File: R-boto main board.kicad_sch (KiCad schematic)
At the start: 1 part

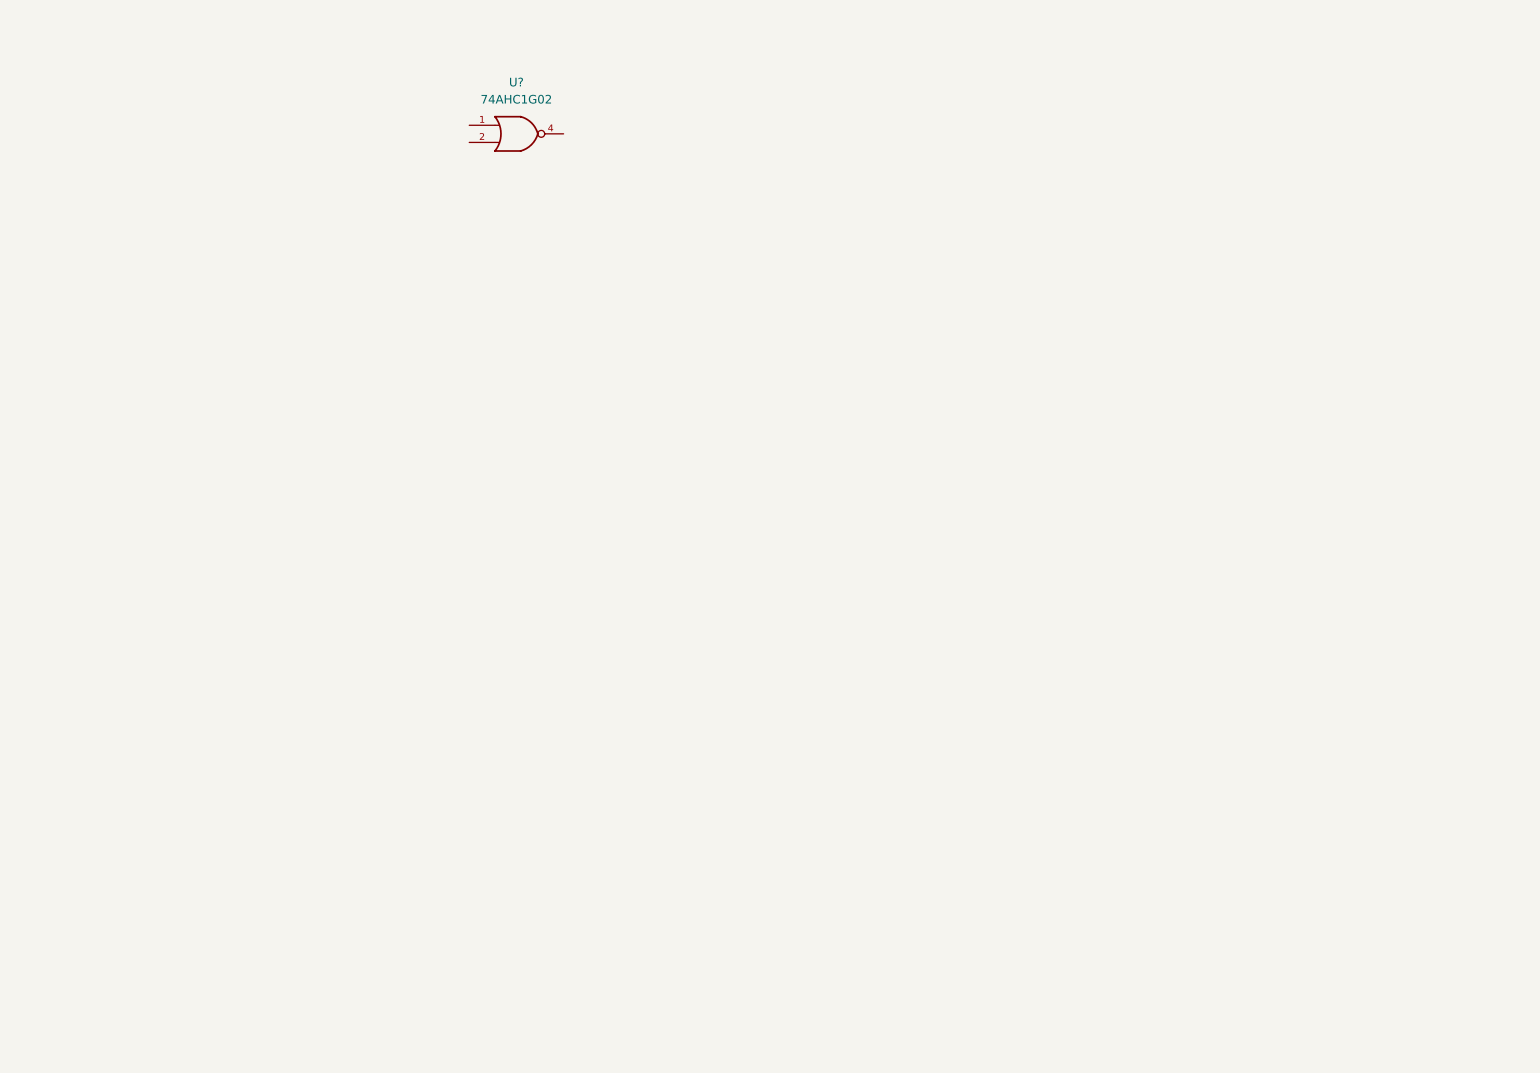
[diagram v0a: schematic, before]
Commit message: schematic connector add
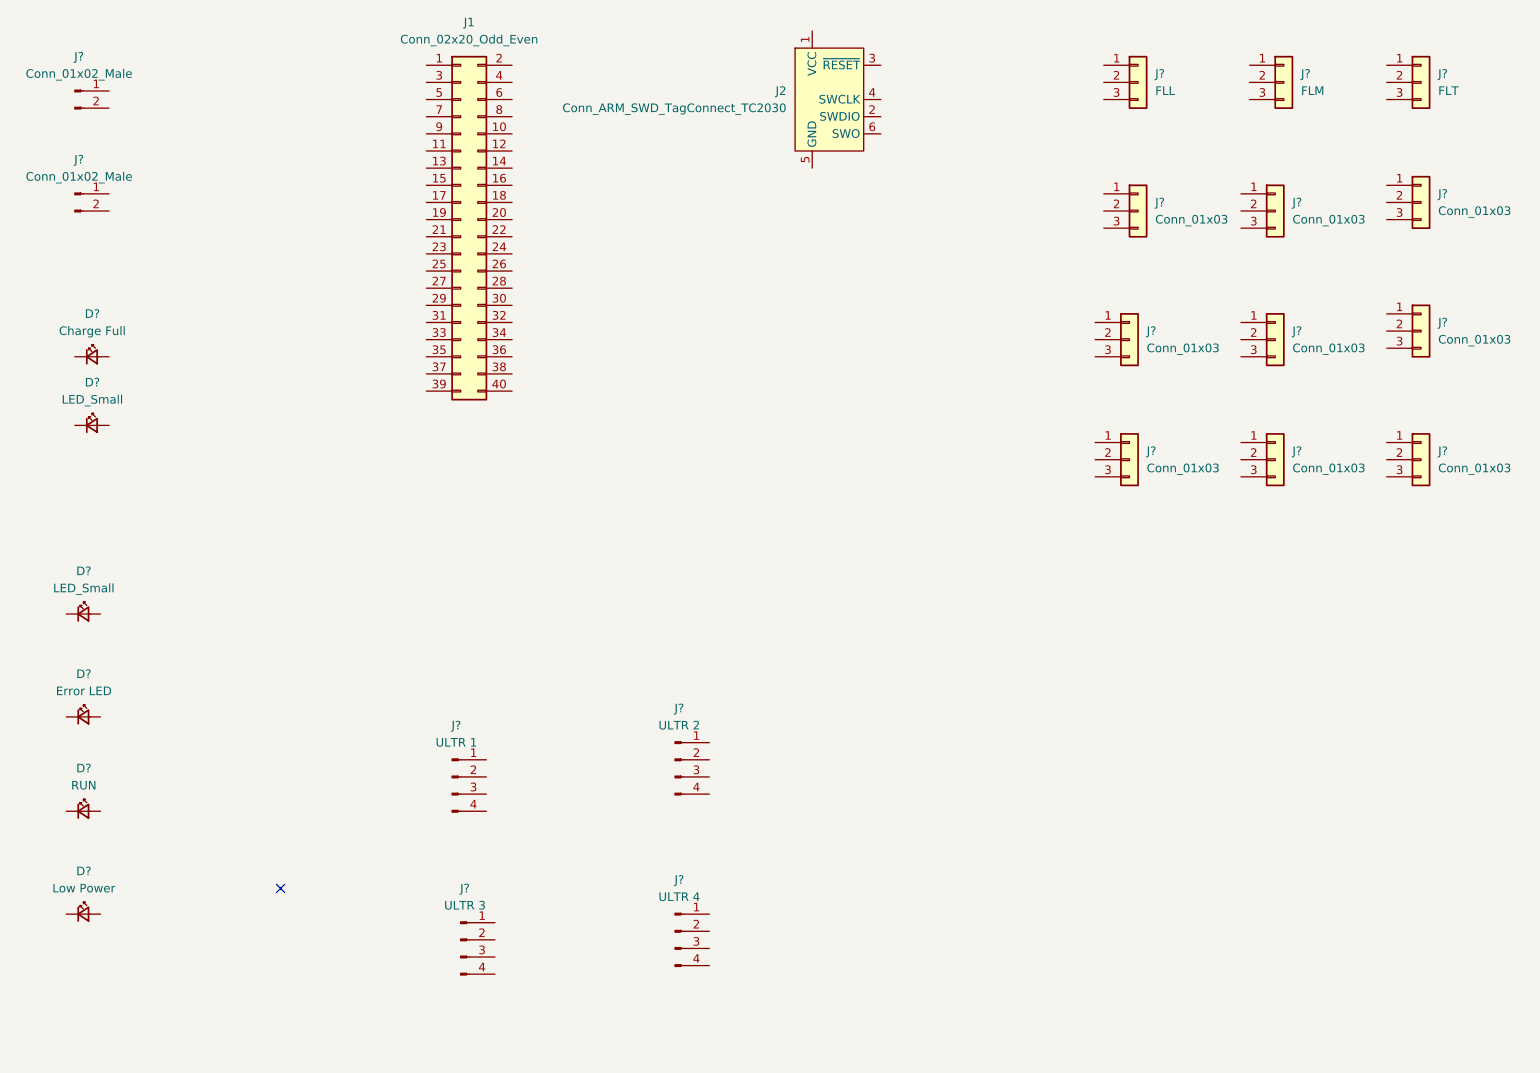
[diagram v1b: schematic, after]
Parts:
- removed U?: 74AHC1G02, symbol 74xGxx:74AHC1G02
- added D?: Charge Full, symbol Device:LED_Small
- added D? (x2): LED_Small, symbol Device:LED_Small
- added D?: Error LED, symbol Device:LED_Small
- added D?: Low Power, symbol Device:LED_Small
- added D?: RUN, symbol Device:LED_Small
- added J1: Conn_02x20_Odd_Even, symbol Connector_Generic:Conn_02x20_Odd_Even
- added J2: Conn_ARM_SWD_TagConnect_TC2030, Connector:Tag-Connect_TC2030-IDC-FP_2x03_P1.27mm_Vertical, symbol Connector:Conn_ARM_SWD_TagConnect_TC2030
- added J? (x9): Conn_01x03, symbol Connector_Generic:Conn_01x03
- added J?: FLL, symbol Connector_Generic:Conn_01x03
- added J?: FLM, symbol Connector_Generic:Conn_01x03
- added J?: ULTR 3, symbol Connector:Conn_01x04_Male
- added J?: ULTR 2, symbol Connector:Conn_01x04_Male
- added J?: FLT, symbol Connector_Generic:Conn_01x03
- added J? (x2): Conn_01x02_Male, symbol Connector:Conn_01x02_Male
- added J?: ULTR 4, symbol Connector:Conn_01x04_Male
- added J?: ULTR 1, symbol Connector:Conn_01x04_Male
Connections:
- no-connect marks 0 -> 1

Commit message: component placing
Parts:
- added BZ1: Buzzer, Buzzer_Beeper:MagneticBuzzer_PUI_AT-0927-TT-6-R, symbol Device:Buzzer
- added D7: DATA, LED_SMD:LED_0805_2012Metric_Pad1.15x1.40mm_HandSolder, symbol Device:LED_Small
- added J21: OLED, jyothu footprint:4pin connector solder pad, symbol Connector:Conn_01x04_Male
- added R1: Ambient Light Sensor, OptoDevice:R_LDR_5.1x4.3mm_P3.4mm_Vertical, symbol Sensor_Optical:LDR07
- D1: renamed from D?; value LED_Small -> BOOT; footprint (none) -> Connector_PinHeader_2.54mm:PinHeader_1x04_P2.54mm_Vertical
- D2: renamed from D?; value Error LED -> ERROR; footprint (none) -> LED_SMD:LED_0805_2012Metric_Pad1.15x1.40mm_HandSolder
- D3: renamed from D?; footprint (none) -> LED_SMD:LED_0805_2012Metric_Pad1.15x1.40mm_HandSolder
- D4: renamed from D?; value Low Power -> BAT LOW; footprint (none) -> LED_SMD:LED_0805_2012Metric_Pad1.15x1.40mm_HandSolder
- D5: renamed from D?; value Charge Full -> CHARGING; footprint (none) -> LED_SMD:LED_0805_2012Metric_Pad1.15x1.40mm_HandSolder
- D6: renamed from D?; value LED_Small -> BAT FULL; footprint (none) -> LED_SMD:LED_0805_2012Metric_Pad1.15x1.40mm_HandSolder
- J1: value Conn_02x20_Odd_Even -> GPIO; footprint (none) -> Connector_PinHeader_2.54mm:PinHeader_2x20_P2.54mm_Vertical
- J10: renamed from J?; value Conn_01x03 -> BRL; footprint (none) -> jyothu footprint:3 pin connector solder pad
- J11, J16, J17: renamed from J?; footprint (none) -> jyothu footprint:3 pin connector solder pad
- J12: renamed from J?; value Conn_01x03 -> BLL; footprint (none) -> jyothu footprint:3 pin connector solder pad
- J13: renamed from J?; value Conn_01x03 -> BLM; footprint (none) -> jyothu footprint:3 pin connector solder pad
- J14: renamed from J?; value Conn_01x03 -> FRM; footprint (none) -> jyothu footprint:3 pin connector solder pad
- J15: renamed from J?; value Conn_01x03 -> BRM; footprint (none) -> jyothu footprint:3 pin connector solder pad
- J18: renamed from J?; value Conn_01x03 -> BLT; footprint (none) -> jyothu footprint:3 pin connector solder pad
- J19: renamed from J?; value Conn_01x03 -> FRT; footprint (none) -> jyothu footprint:3 pin connector solder pad
- J2: value Conn_ARM_SWD_TagConnect_TC2030 -> SWD
- J20: renamed from J?; value Conn_01x03 -> BRT; footprint (none) -> jyothu footprint:3 pin connector solder pad
- J3: renamed from J?; value Conn_01x02_Male -> 3.3V IN; footprint (none) -> Connector_PinHeader_2.54mm:PinHeader_1x02_P2.54mm_Vertical
- J4: renamed from J?; value Conn_01x02_Male -> 5V IN; footprint (none) -> Connector_PinHeader_2.54mm:PinHeader_1x02_P2.54mm_Vertical
- J5, J6, J7, J8: renamed from J?; footprint (none) -> jyothu footprint:4pin connector solder pad
- J9: renamed from J?; value Conn_01x03 -> FRL; footprint (none) -> jyothu footprint:3 pin connector solder pad
